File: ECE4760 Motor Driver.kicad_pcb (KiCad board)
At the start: 6 copper layers, 43.2 x 52.1 mm, 160 parts, among them J1 IO, J100 Alternative Motor, J2 Motor / Power, J3 USB_B_Micro, J4 UART, J5 Debug, Q1 EPC23104, Q2 EPC23104, Q3 EPC23104, Q4 EPC23104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

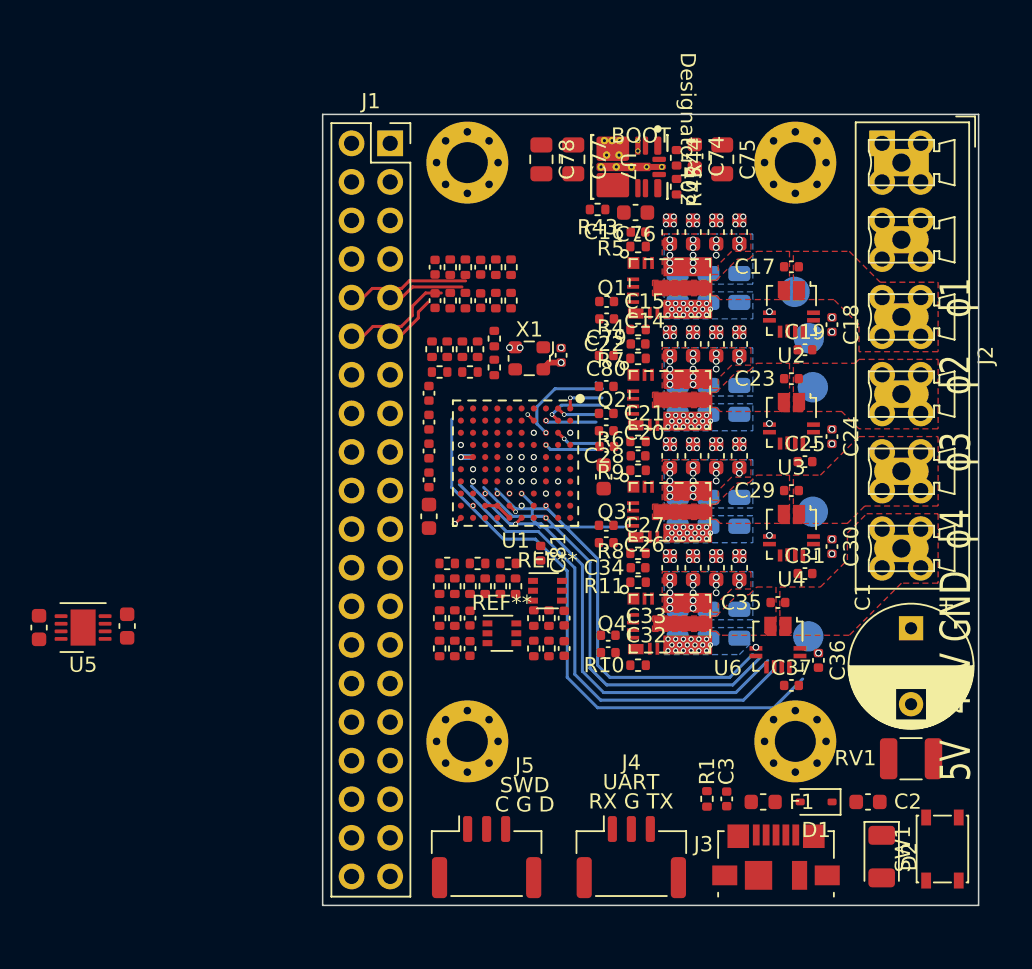
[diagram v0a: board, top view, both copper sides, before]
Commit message: Updated routing
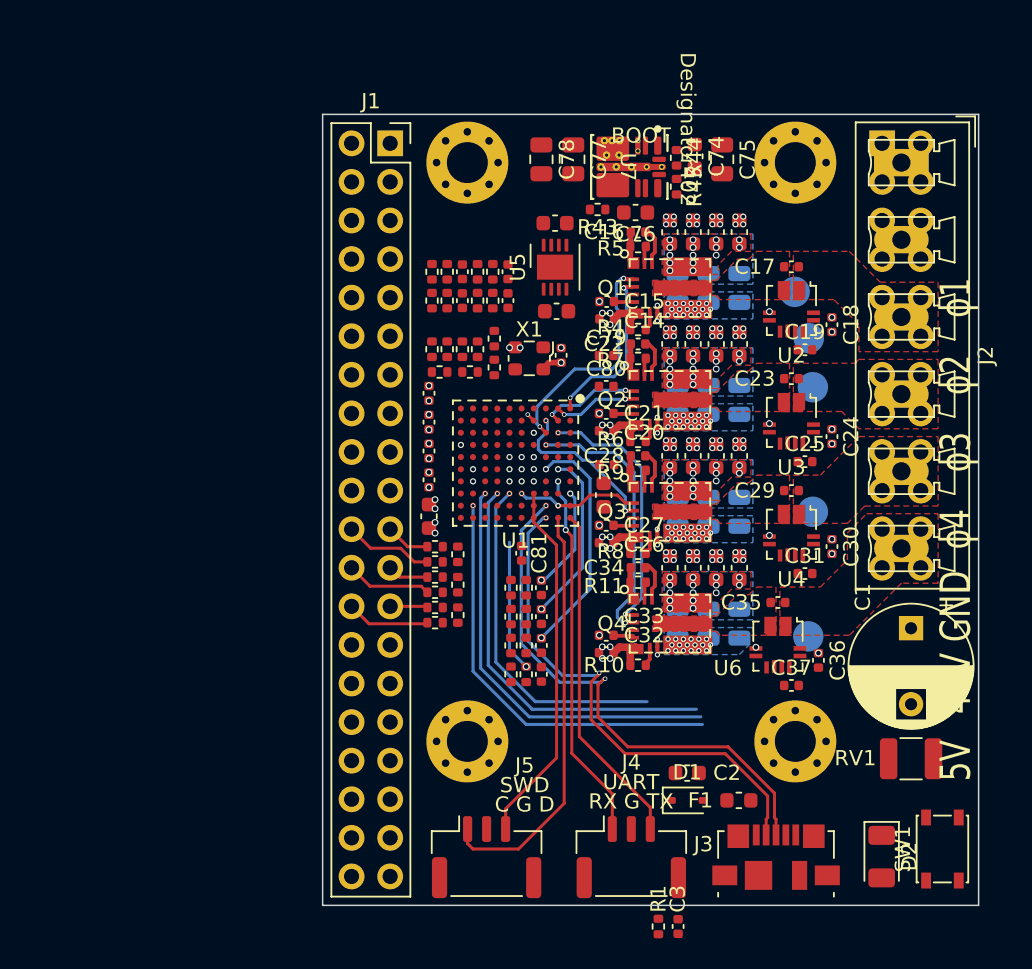
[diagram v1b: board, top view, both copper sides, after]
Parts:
- removed REF** (x2): SOT-363_SC-70-6, Package_TO_SOT_SMD:SOT-363_SC-70-6
- moved C12 43.2 mm to (91.5, 47.8), turned to 0 degrees
- moved U5 39.1 mm to (91.5, 50.7), turned to 90 degrees
- moved C13 35.1 mm to (91.6, 53.6), turned to 0 degrees
- moved C2 12.1 mm to (100.2, 84.0)
- moved C3 8.99 mm to (99.6, 94.1)
- moved R1 8.99 mm to (98.3, 94.1)
- moved D1 8.49 mm to (100.2, 85.8), turned to 0 degrees
- moved R26 5.82 mm to (83.6, 74.1), turned to 0 degrees
- moved R35 5.54 mm to (83.4, 51.0), turned to 90 degrees
- moved C73 5.28 mm to (88.4, 52.9), turned to -90 degrees
- moved C66 5.03 mm to (90.6, 75.6)
- moved R12 5.03 mm to (88.6, 75.6)
- moved R13 5.03 mm to (89.6, 75.6)
- moved C69 5.00 mm to (90.6, 77.5)
- moved R18 5.00 mm to (88.6, 77.5)
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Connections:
- C70 pad 1: /LIM_L -> /Limit Switch Input1/Out
- C71 pad 1: /LIM_R -> /Limit Switch Input2/Out
- C72 pad 1: /LIM_H -> /Limit Switch Input3/Out
- C73 pad 1: /LIM_AUX -> /Limit Switch Input4/Out
- J1 pad 29: Lim_H_In -> Hall_B_In
- J1 pad 3: Hall_B_In -> Lim_H_In
- J1 pad 30: Lim_L_In -> Hall_C_In
- J1 pad 31: Lim_Aux_In -> Hall_A_In
- J1 pad 32: Lim_R_In -> Hall_I_In
- J1 pad 4: Hall_C_In -> Lim_L_In
- J1 pad 5: Hall_A_In -> Lim_Aux_In
- J1 pad 6: Hall_I_In -> Lim_R_In
- R35 pad 2: /LIM_L -> /Limit Switch Input1/Out
- R36 pad 2: /LIM_L -> /Limit Switch Input1/Out
- R37 pad 2: /LIM_R -> /Limit Switch Input2/Out
- R38 pad 2: /LIM_R -> /Limit Switch Input2/Out
- R39 pad 2: /LIM_H -> /Limit Switch Input3/Out
- R40 pad 2: /LIM_H -> /Limit Switch Input3/Out
- R41 pad 2: /LIM_AUX -> /Limit Switch Input4/Out
- R42 pad 2: /LIM_AUX -> /Limit Switch Input4/Out
- U1 pad A5: /HALL_A -> unconnected-(U1-PB3-PadA5)
- U1 pad A6: /HALL_C -> unconnected-(U1-PD6-PadA6)
- U1 pad A7: unconnected-(U1-PD5-PadA7) -> /UART_RX
- U1 pad A9: unconnected-(U1-PD1-PadA9) -> /PH3_HI
- U1 pad B5: /HALL_A -> unconnected-(U1-PB5-PadB5)
- U1 pad B9: unconnected-(U1-PA15-PadB9) -> /PH3_HI
- U1 pad C8: /LIM_AUX -> unconnected-(U1-PC10-PadC8)
- U1 pad E10: /LIM_H -> unconnected-(U1-PA8-PadE10)
- U1 pad E9: /LIM_R -> unconnected-(U1-PC9-PadE9)
- U1 pad F10: /ENC_I+ -> unconnected-(U1-PC7-PadF10)
- U1 pad F9: /LIM_L -> unconnected-(U1-PC6-PadF9)
- U1 pad G9: /ENC_I+ -> unconnected-(U1-PD13-PadG9)
- U1 pad J3: /AUX_ENC_A+ -> unconnected-(U1-PC5-PadJ3)
- U1 pad K2: /AUX_ENC_A- -> unconnected-(U1-PC4-PadK2)
- U1 pad K3: /AUX_ENC_A+ -> unconnected-(U1-PB1-PadK3)
- U1 pad K8: /ENC_A- -> unconnected-(U1-PB12-PadK8)
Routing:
- net +3V3: track 43.3 -> 3.12 mm, vias 11 -> 16
- net /USB_D+: track 0.00 -> 35.7 mm, vias 1 -> 2
- net /USB_D-: track 0.00 -> 34.0 mm, vias 1 -> 2
- net /SWCLK: track 0.00 -> 27.7 mm
- net /UART_RX: track 0.00 -> 24.4 mm, vias 1 -> 2
- net /SWDIO: track 0.00 -> 24.1 mm
- net /UART_TX: track 0.00 -> 22.7 mm
- net /HALL_A: track 0.00 -> 15.4 mm, vias 0 -> 2
- net /PH4_HI: track 2.89 -> 17.1 mm, vias 1 -> 2
- net /PH4_LO: track 3.82 -> 17.8 mm, vias 1 -> 2
- net Aux_Enc_B_In-: track 13.3 -> 0.00 mm
- net /HALL_C: track 0.00 -> 11.4 mm, vias 0 -> 2
- net Aux_Enc_A_In+: track 11.7 -> 0.35 mm
- net +5V: track 0.00 -> 11.1 mm, vias 0 -> 8
- net /HALL_I: track 0.00 -> 8.65 mm, vias 0 -> 1
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- added copper zone on In1.Cu, net GND
- added copper zone on In3.Cu, net GND
- removed copper zone on In1.Cu, net +5V
- removed copper zone on In3.Cu, net +5V

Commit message: Power supply and remove USB
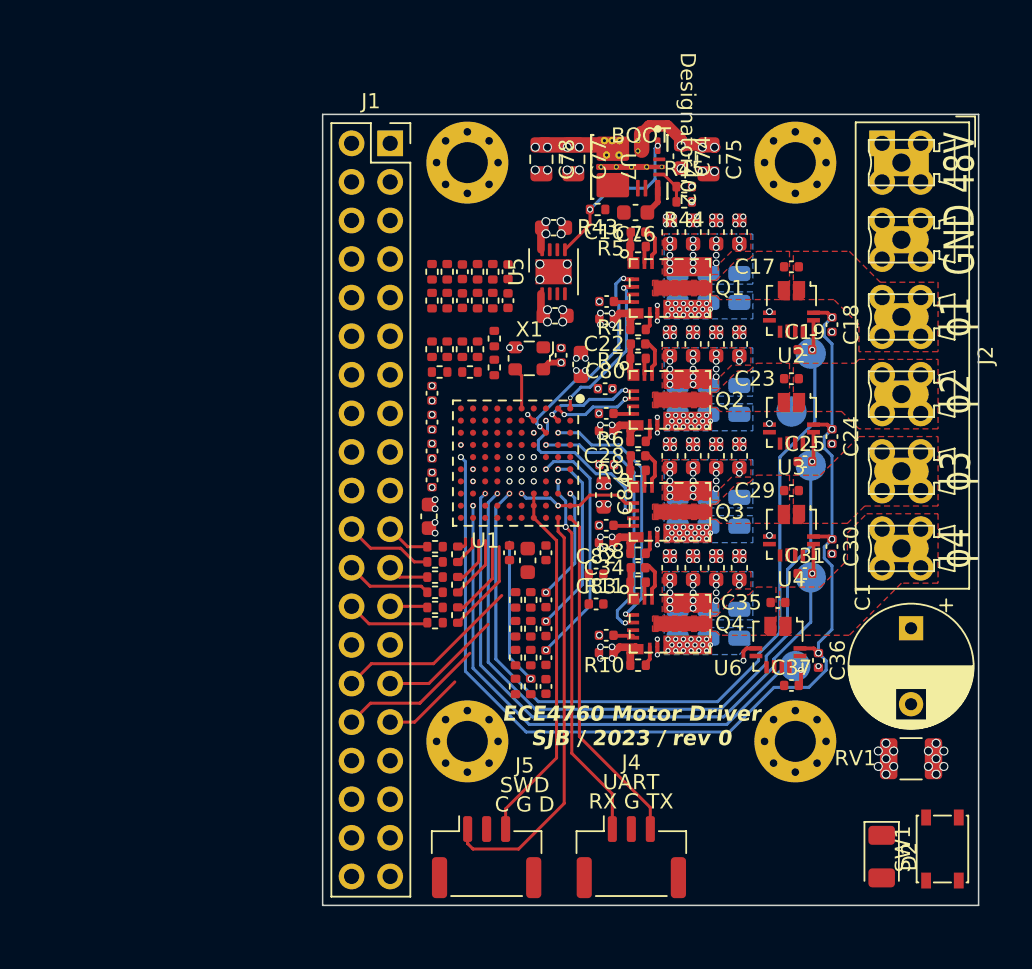
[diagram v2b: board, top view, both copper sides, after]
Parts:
- removed C2: 1u, Capacitor_SMD:C_0603_1608Metric
- removed C3: 100n, Capacitor_SMD:C_0402_1005Metric
- removed D1: 1A, Diode_SMD:D_SOD-323
- removed F1: 1A, Fuse:Fuse_0603_1608Metric
- removed J3: USB_B_Micro, Connector_USB:USB_Micro-B_Molex_47346-0001
- removed R1: 1k, Resistor_SMD:R_0402_1005Metric
- added C82: 100n, Capacitor_SMD:C_0402_1005Metric, F.Cu at (94.2, 70.9)
- added C83: 100n, Capacitor_SMD:C_0402_1005Metric, F.Cu at (94.2, 72.9)
- added C84: 1u, Capacitor_SMD:C_0603_1608Metric, F.Cu at (94.7, 65.7)
- added C85: 1u, Capacitor_SMD:C_0603_1608Metric, F.Cu at (93.2, 57.1)
- moved C79 13.6 mm to (90.9, 69.5), turned to -90 degrees
- moved C5 6.59 mm to (89.7, 70.0)
- moved TP2 5.16 mm to (108.3, 63.8)
- moved TP5 4.96 mm to (107.1, 60.2)
- moved TP3 4.32 mm to (108.3, 71.1)
- moved TP1 4.20 mm to (108.3, 56.4)
- moved R44 2.94 mm to (100.0, 46.4), turned to 180 degrees
- moved TP4 2.14 mm to (107.3, 77.0)
- moved C74 0.90 mm to (99.8, 43.4)
- moved C75 0.90 mm to (101.6, 43.6)
- moved C66 0.85 mm to (90.9, 76.4)
- moved R12 0.85 mm to (88.9, 76.4)
- moved R13 0.85 mm to (89.9, 76.4)
- moved C67 0.85 mm to (90.9, 72.6)
- moved C68 0.85 mm to (90.9, 74.5)
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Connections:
- C18 pad 2: +3V3 -> VREF
- C24 pad 2: +3V3 -> VREF
- C30 pad 2: +3V3 -> VREF
- C36 pad 2: +3V3 -> VREF
- J1 pad 29: Hall_B_In -> Hall_C_In
- J1 pad 30: Hall_C_In -> Hall_B_In
- J1 pad 31: Hall_A_In -> Hall_I_In
- J1 pad 32: Hall_I_In -> Hall_A_In
- U1 pad A7: /UART_RX -> unconnected-(U1-PD5-PadA7)
- U1 pad C10: /USB_D- -> unconnected-(U1-PA11-PadC10)
- U1 pad C9: /USB_D+ -> unconnected-(U1-PA12-PadC9)
- U1 pad K5: +3V3 -> VREF
- U2 pad 10: +3V3 -> VREF
- U3 pad 10: +3V3 -> VREF
- U4 pad 10: +3V3 -> VREF
- U6 pad 10: +3V3 -> VREF
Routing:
- net VREF: track 0.00 -> 71.7 mm, vias 0 -> 5
- net /USB_D+: track 35.7 -> 0.00 mm, vias 2 -> 0
- net /USB_D-: track 34.0 -> 0.00 mm, vias 2 -> 0
- net /PH1_SENSE: track 22.5 -> 54.7 mm, vias 1 -> 2
- net /PH2_SENSE: track 26.4 -> 48.4 mm, vias 1 -> 2
- net /PH3_SENSE: track 27.4 -> 42.4 mm, vias 1 -> 2
- net Hall_B_In: track 0.00 -> 12.3 mm
- net Net-(U5-EN): track 0.00 -> 10.7 mm, vias 0 -> 2
- net Hall_A_In: track 0.00 -> 9.66 mm
- net +5V: track 11.1 -> 20.0 mm, vias 8 -> 15
- net /PH4_SENSE: track 27.4 -> 36.1 mm, vias 1 -> 2
- net Hall_C_In: track 0.00 -> 8.06 mm
- net Vdrive: track 0.00 -> 7.96 mm, vias 60 -> 74
- net /ENC_I+: track 0.00 -> 6.14 mm
- net Hall_I_In: track 0.00 -> 5.35 mm
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- added copper zone on In4.Cu, net GND
- removed copper zone on In4.Cu, net +5V
- removed copper zone on In3.Cu, net Aux_Enc_A_In-
- removed copper zone on In4.Cu, net Aux_Enc_A_In-
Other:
- board text added: "ECE4760 Motor Driver SJB / 2023 / rev 0"
